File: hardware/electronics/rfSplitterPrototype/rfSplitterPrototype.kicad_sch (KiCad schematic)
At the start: 43 parts, among them J1 PRPC002SBAN-M71RC, U1 TPS7A16A-Q1, U2 PMA2-162LNA+, U3 QCN-19D+

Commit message: worked on RF splitter
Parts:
- removed J1: PRPC002SBAN-M71RC, lib_fp:conn_01x02_254_right_angle, symbol DS-Connectors:Conn_01x02_Pin
- added C10: 100pF, lib_fp:GCM0402, symbol lib_sch:C
- added C11: 100nF, lib_fp:GCM0402, symbol lib_sch:C
- added C13: 470pF, lib_fp:GCM0402, symbol lib_sch:C_horizontal
- added J2: VAL, lib_fp:conn_01x03_254_right_angle, symbol DS-Connectors:Conn_01x03_Pin
- added L2: 68nH, lib_fp:L_0402, symbol lib_sch:L
- added NT1: NetTie, lib_fp:NetTie-2_SMD_Pad1.0mm, symbol lib_sch:NetTie
- added TP12: ~, lib_fp:TP_2mm, symbol lib_sch:Testpoint
- TP9: value RCWCTE -> ~; footprint lib_fp:TP_RCW -> lib_fp:TP_2mm; DKPN 2019-RCWCTECT-ND -> N/A; MPN RCWCTE -> N/A; Manufacturer KOA Speer Electronics, Inc. -> N/A
- renumbered C10 to C12, C11 to C14, C12 to C15, C13 to C16, L2 to L3, TP2 to TP1, TP1 to TP2
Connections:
- net AGND is gone; now on net VSS: C16.2, R6.2, TP10.1, U2.1 (NC), U2.6 (NC), U2.8 (GND), U2.9 (GND), U3.2 (GND), U3.5 (GND)
- net GND: now also J2.3, NT1.1
- net GNSS_RF-IN: now also TP9.1, C13.1, L2.2; no longer C14.1, TP6.1
- net LNA_RF-GND: no longer TP9.1
- net VIN: now also J2.1
- net VSS: now also C10.2, C11.2, NT1.2
- new net: C13.2, C14.1, TP6.1
- new net +3V3: C10.1, C11.1, J2.2, L2.1, TP12.1
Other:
- moved on the sheet: AE1, C1, C2, C3, C4, C5, C6, R1, R2, R3, TP1, U1

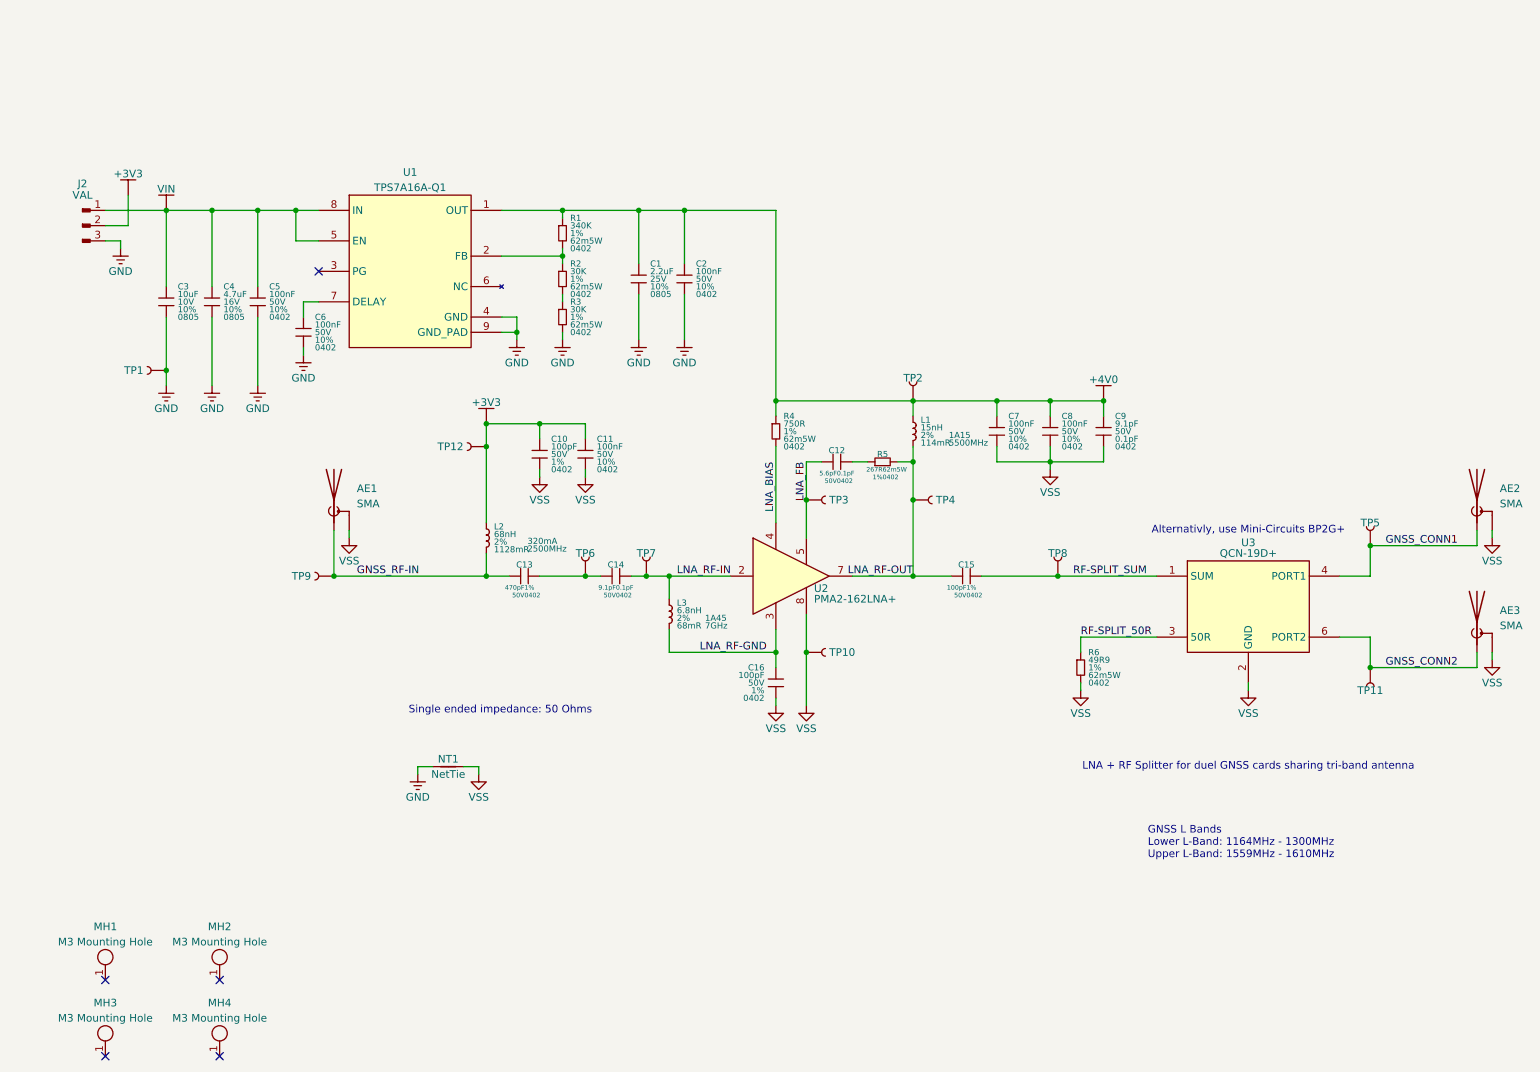
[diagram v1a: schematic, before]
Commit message: updated with new LNA
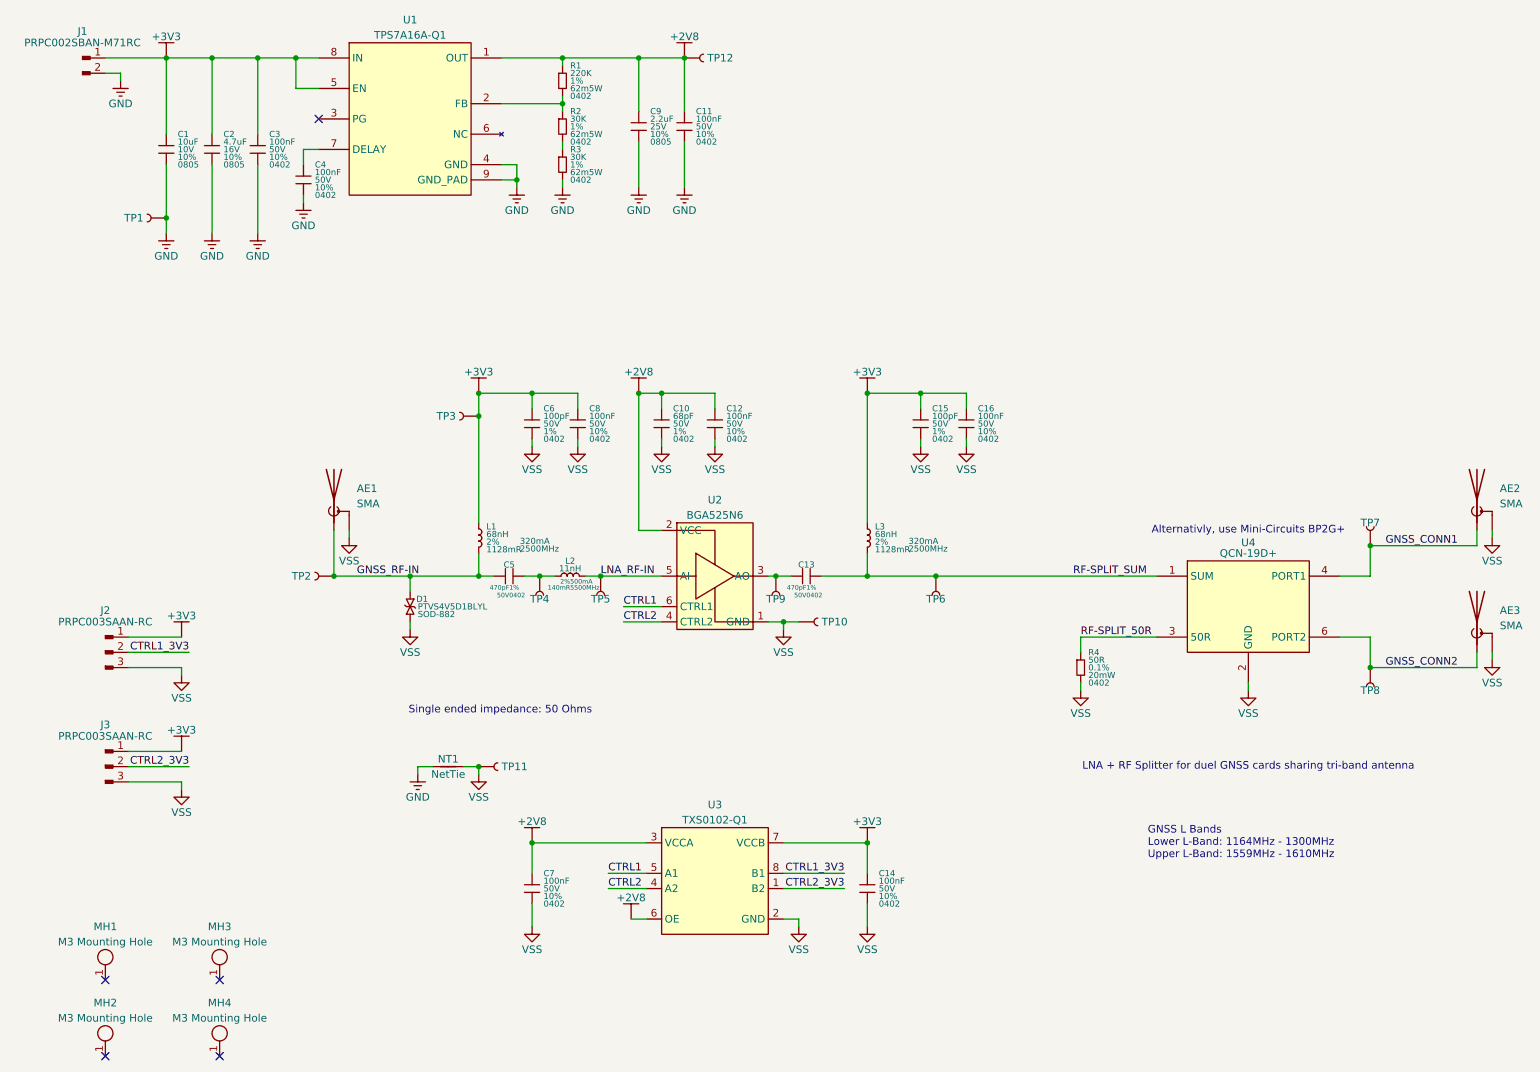
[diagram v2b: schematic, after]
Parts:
- removed C12: 5.6pF, lib_fp:GCM0402, symbol lib_sch:C_horizontal
- removed C14: 9.1pF, lib_fp:GCM0402, symbol lib_sch:C_horizontal
- removed C15: 100pF, lib_fp:GCM0402, symbol lib_sch:C_horizontal
- removed C8: 100nF, lib_fp:GCM0402, symbol lib_sch:C
- removed C9: 9.1pF, lib_fp:GCM0402, symbol lib_sch:C
- removed J2: VAL, lib_fp:conn_01x03_254_right_angle, symbol DS-Connectors:Conn_01x03_Pin
- removed L1: 15nH, lib_fp:L_0402, symbol lib_sch:L
- removed R4: 750R, lib_fp:CRCW0402, symbol lib_sch:R
- removed R5: 267R, lib_fp:CRCW0402, symbol lib_sch:R_horizontal
- removed TP2, TP3, TP4, TP7, TP8: ~, lib_fp:TP_2mm, symbol lib_sch:Testpoint
- removed U2: PMA2-162LNA+, lib_fp:TFDFN200X200X100-8, symbol lib_sch:PMA2-162LNA+
- added C10: 68pF, lib_fp:GCM0402, symbol lib_sch:C
- added C12, C14: 100nF, lib_fp:GCM0402, symbol lib_sch:C
- added C13: 470pF, lib_fp:GCM0402, symbol lib_sch:C_horizontal
- added C15: 100pF, lib_fp:GCM0402, symbol lib_sch:C
- added D1: PTVS4V5D1BLYL, lib_fp:SOD882, symbol lib_sch:D_TVS
- added J1: PRPC002SBAN-M71RC, DS-Rectangular-Connectors:conn_01x02_254_right_angle, symbol lib_sch:Conn_01x02_Pin
- added J2, J3: PRPC003SAAN-RC, DS-Rectangular-Connectors:conn_01x03_254, symbol lib_sch:Conn_01x03_Pin
- added L2: 11nH, lib_fp:L_0402, symbol lib_sch:L_horizontal
- added TP11: RCWCTE, lib_fp:TP_RCW, symbol lib_sch:Testpoint
- added TP12, TP5, TP6, TP9: ~, lib_fp:TP_2mm, symbol lib_sch:Testpoint
- added U2: BGA525N6, lib_fp:XDFN110X70X37-6, symbol lib_sch:BGA525N6
- added U3: TXS0102-Q1, lib_fp:VSSOP50P310X90-8, symbol lib_sch:TXS0102
- AE1, AE2, AE3: footprint lib_fp:CONSMA002-G -> lib_fp:0732511153
- C16: value 100pF -> 100nF; DKPN 490-14349-1-ND -> 490-GRT155R71H104KE01DCT-ND; MPN GCM1555C1H101FA16D -> GRT155R71H104KE01D; Tolerance 1% -> 10%
- L3: value 6.8nH -> 68nH; Current Rating 1A45 -> 320mA; DC Resistance 68mR -> 1128mR; DKPN 490-15561-1-ND -> 490-15537-1-ND; MPN LQW15AN6N8G8ZD -> LQW15AN68NG8ZD; Resonant Frequency 7GHz -> 2500MHz
- R1: value 340K -> 220K; DKPN 541-340KLCT-ND -> 541-220KLCT-ND; MPN CRCW0402340KFKED -> CRCW0402220KFKED
- R4: renamed from R6; value 49R9 -> 50R; DKPN 541-49.9LCT-ND -> FC0402-50BWCT-ND; MPN CRCW040249R9FKED -> FC0402E50R0BST1; Manufacturer Vishay Dale -> Vishay Dale Thin Film; Power Rating 62m5W -> 20mW; Tolerance 1% -> 0.1%
- renumbered C3 to C1, C2 to C11, C4 to C2, C5 to C3, C6 to C4, C13 to C5, C10 to C6, C11 to C8, C1 to C9, L2 to L1, MH3 to MH2, MH2 to MH3, TP9 to TP2, TP12 to TP3, TP6 to TP4, TP5 to TP7, TP11 to TP8, U3 to U4
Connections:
- net VIN is gone; now on net +3V3: C1.1, C2.1, C3.1, U1.5 (EN), U1.8 (IN)
- net +3V3: now also C16.1, L3.1, C14.1, C15.1, J1.1, J2.1, J3.1, U3.7 (VCCB)
- net GND: now also J1.2
- net GNSS_RF-IN: now also D1.2
- net LNA_RF-IN: now also L2.2, TP5.1, U2.5 (AI); no longer L3.1
- net RF-SPLIT_SUM: now also L3.2, C13.2, TP6.1
- net VSS: now also C10.2, C12.2, C14.2, C15.2, D1.1, J2.3, J3.3, TP11.1, U2.1 (GND), U3.2 (GND); no longer AE1.3 (Shield), AE1.4 (Shield), AE1.5 (Shield), AE2.3 (Shield), AE2.4 (Shield), AE2.5 (Shield), AE3.3 (Shield), AE3.4 (Shield), AE3.5 (Shield)
- net at C5.2, TP4.1: now also L2.1
- net +4V0 renamed +2V8
- net +2V8: now also C10.1, C12.1, TP12.1, U2.2 (VCC), U3.3 (VCCA), U3.6 (OE)
- removed net LNA_RF-GND: C16.1, L3.2
- new net: C13.1, TP9.1, U2.3 (AO)
- new net CTRL1: U2.6 (CTRL1), U3.5 (A1)
- new net CTRL1_3V3: J2.2, U3.8 (B1)
- new net CTRL2: U2.4 (CTRL2), U3.4 (A2)
- new net CTRL2_3V3: J3.2, U3.1 (B2)
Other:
- moved on the sheet: C1, C11, C2, C3, C4, C5, C6, C8, C9, L1, R1, R2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
